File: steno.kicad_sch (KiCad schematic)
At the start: 9 parts, among them SW1 SW_Push, SW2 SW_Push, SW3 SW_Push, SW4 SW_Push, SW5 SW_Push, SW6 SW_Push, SW7 SW_Push, SW8 SW_Push

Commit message: Continue schematic
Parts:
- added SW10, SW11, SW12, SW13, SW14, SW15, SW16, SW17, SW18, SW19, SW20, SW21, SW22, SW23, SW24, SW9: SW_Push, symbol Switch:SW_Push
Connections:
- net S0: now reaches A1.1 (GPIO0)
- net S0: now also SW1.2
- net H: now reaches A1.10 (GPIO7)
- net H: now also SW9.1
- net R: now reaches A1.11 (GPIO8)
- net R: now also SW10.1
- net STAR0: now reaches A1.12 (GPIO9)
- net STAR0: now also SW11.2
- net -A-: now reaches A1.14 (GPIO10)
- net -O-: now reaches A1.15 (GPIO11)
- net -E-: now reaches A1.16 (GPIO12)
- net -U-: now reaches A1.17 (GPIO13)
- net -F: now reaches A1.19 (GPIO14)
- net -F: now also SW20.1
- net S1: now reaches A1.2 (GPIO1)
- net S1: now also SW3.2
- net -R: now reaches A1.20 (GPIO15)
- net -R: now also SW21.1
- net STAR1: now reaches A1.21 (GPIO16)
- net STAR1: now also SW22.2
- net -B: now reaches A1.22 (GPIO17)
- net -B: now also SW18.2
- net -P: now reaches A1.24 (GPIO18)
- net -P: now also SW17.2
- net -G: now reaches A1.25 (GPIO19)
- net -G: now also SW16.1
- net -L: now reaches A1.26 (GPIO20)
- net -L: now also SW15.1
- net -S: now reaches A1.27 (GPIO21)
- net -S: now also SW13.2
- net -T: now reaches A1.29 (GPIO22)
- net -T: now also SW12.2
- net NUM2-3: now reaches A1.31 (GPIO26_ADC0)
- net -Z: now reaches A1.32 (GPIO27_ADC1)
- net -Z: now also SW24.1
- net -D: now reaches A1.34 (GPIO28_ADC2)
- net -D: now also SW23.1
- net T: now reaches A1.4 (GPIO2)
- net T: now also SW4.1
- net K: now reaches A1.5 (GPIO3)
- net K: now also SW5.1
- net NUM0-1: now reaches A1.6 (GPIO4)
- net NUM0-1: now also SW2.2, SW8.1
- net P: now reaches A1.7 (GPIO5)
- net P: now also SW6.2
- net W: now reaches A1.9 (GPIO6)
- net W: now also SW7.2
- net GND: now reaches SW7.1
- net GND: now also SW1.1, SW2.1, SW3.1, SW4.2, SW5.2, SW6.1, SW8.2, SW10.2, SW11.1, SW19.2, SW20.2, SW21.2, SW22.1, SW9.2
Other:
- moved on the sheet: A1, SW1, SW2, SW3, SW4, SW5

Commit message: Start routing
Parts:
- added SW25, SW26, SW27, SW28: SW_Push, Button_Switch_Keyboard:SW_Cherry_MX_1.00u_PCB, symbol Switch:SW_Push
- A1: footprint Module_RaspberryPi_Pico:RaspberryPi_Pico_Common -> PiPico:RaspberryPi_Pico_Common_THT
- SW1, SW10, SW12, SW13, SW15, SW16, SW17, SW18, SW20, SW21, SW23, SW24, SW3, SW4, SW5, SW6, SW7, SW9: footprint (none) -> Button_Switch_Keyboard:SW_Cherry_MX_1.00u_PCB
- SW11, SW14, SW19, SW2, SW22, SW8: footprint (none) -> MX_2U_Modified:SW_Cherry_MX_2.00u_PCB
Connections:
- net -A-: now also SW25.2
- net -D: now also SW23.2; no longer SW23.1
- net -E-: now also SW28.2
- net -F: now also SW20.2; no longer SW20.1
- net -G: now also SW16.2; no longer SW16.1
- net -L: now also SW15.2; no longer SW15.1
- net -O-: now also SW26.2
- net -R: now also SW21.2; no longer SW21.1
- net -U-: now also SW27.2
- net -Z: now also SW24.2; no longer SW24.1
- net GND: now also SW10.1, SW12.1, SW13.1, SW14.1, SW15.1, SW16.1, SW17.1, SW18.1, SW19.1, SW20.1, SW21.1, SW23.1, SW24.1, SW4.1, SW5.1, SW8.1, SW9.1, SW25.1, SW26.1, SW27.1, SW28.1; no longer SW10.2, SW19.2, SW20.2, SW21.2, SW4.2, SW5.2, SW8.2, SW9.2
- net H: now also SW9.2; no longer SW9.1
- net K: now also SW5.2; no longer SW5.1
- net NUM0-1: now also SW8.2; no longer SW8.1
- net NUM2-3: now also SW14.2, SW19.2
- net R: now also SW10.2; no longer SW10.1
- net T: now also SW4.2; no longer SW4.1

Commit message: Finish routing
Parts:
- A1: footprint PiPico:RaspberryPi_Pico_Common_THT -> PiPico:RaspberryPi_Pico_Common
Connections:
- net GND: now also A1.13 (GND), A1.18 (GND), A1.23 (GND), A1.28 (GND), A1.3 (GND), A1.38 (GND), A1.8 (GND)
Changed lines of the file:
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@@
 	(wire
 		(pts
+			(xy 107.95 96.52) (xy 107.95 99.06)
+		)
+		(stroke
+			(width 0)
+			(type default)
+		)
+	)
+	(wire
+		(pts
 			(xy 68.58 125.73) (xy 71.12 125.73)
 		)
@@
 			)
 		)
-		(property "Footprint" "PiPico:RaspberryPi_Pico_Common_THT"
+		(property "Footprint" "PiPico:RaspberryPi_Pico_Common"
 			(at 107.95 107.95 0)
 			(effects
@@
 					(unit 1)
 				)
+			)
+		)
+	)
+	(symbol
+		(lib_id "power:GND")
+		(at 107.95 99.06 0)
+		(unit 1)
+		(exclude_from_sim no)
+		(in_bom yes)
+		(on_board yes)
+		(dnp no)
+		(property "Reference" "#PWR08"
+			(at 107.95 105.41 0)
+			(effects
+				(font
+					(size 1.27 1.27)
+				)
+				(hide yes)
+			)
+		)
+		(property "Value" "GND"
+			(at 107.95 102.87 0)
+			(effects
+				(font
+					(size 1.27 1.27)
+				)
+			)
+		)
+		(property "Footprint" ""
+			(at 107.95 99.06 0)
+			(effects
+				(font
+					(size 1.27 1.27)
+				)
+				(hide yes)
+			)
+		)
+		(property "Datasheet" ""
+			(at 107.95 99.06 0)
+			(effects
+				(font
+					(size 1.27 1.27)
+				)
+				(hide yes)
+			)
+		)
+		(property "Description" "Power symbol creates a global label with name \"GND\" , ground"
+			(at 107.95 99.06 0)
+			(effects
+				(font
+					(size 1.27 1.27)
+				)
+				(hide yes)
+			)
+		)
+		(pin "1"
+		)
+		(instances
+			(project ""
+				(path "/81be89d4-c12a-4c6e-a91b-ff1d6efea102"
+					(reference "#PWR08")
+					(unit 1)
+				)

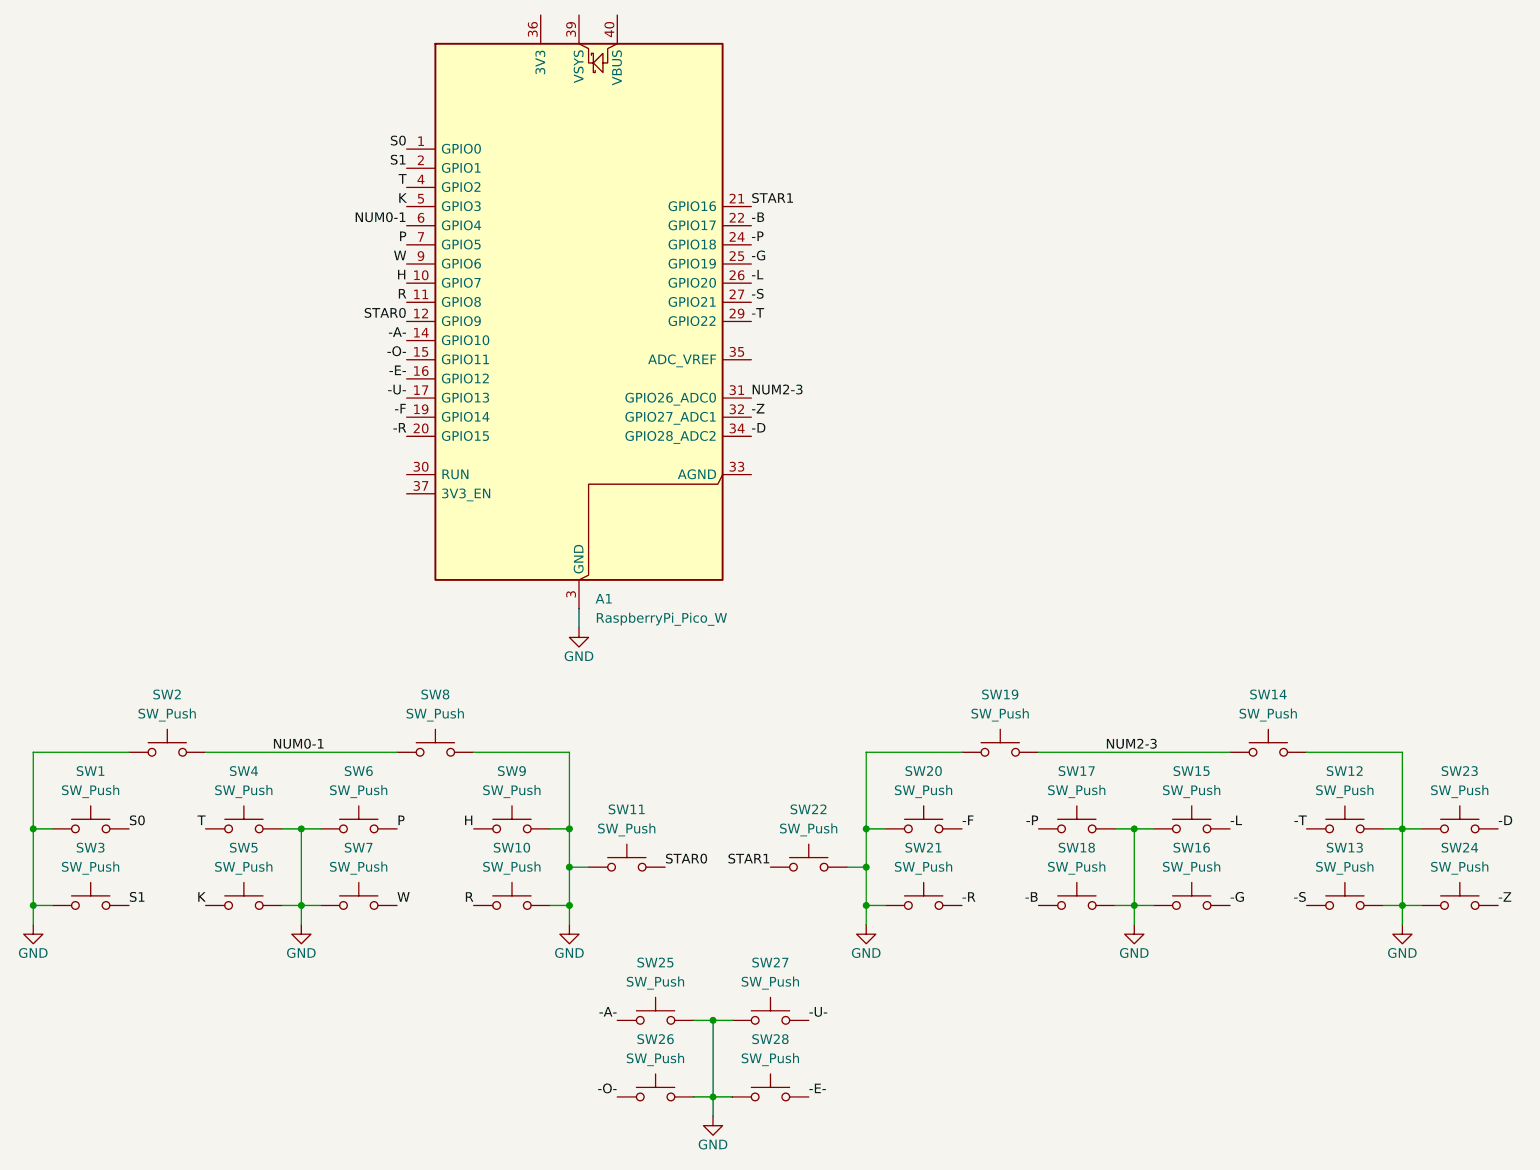
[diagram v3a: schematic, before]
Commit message: Finalized routing, added mounting holes
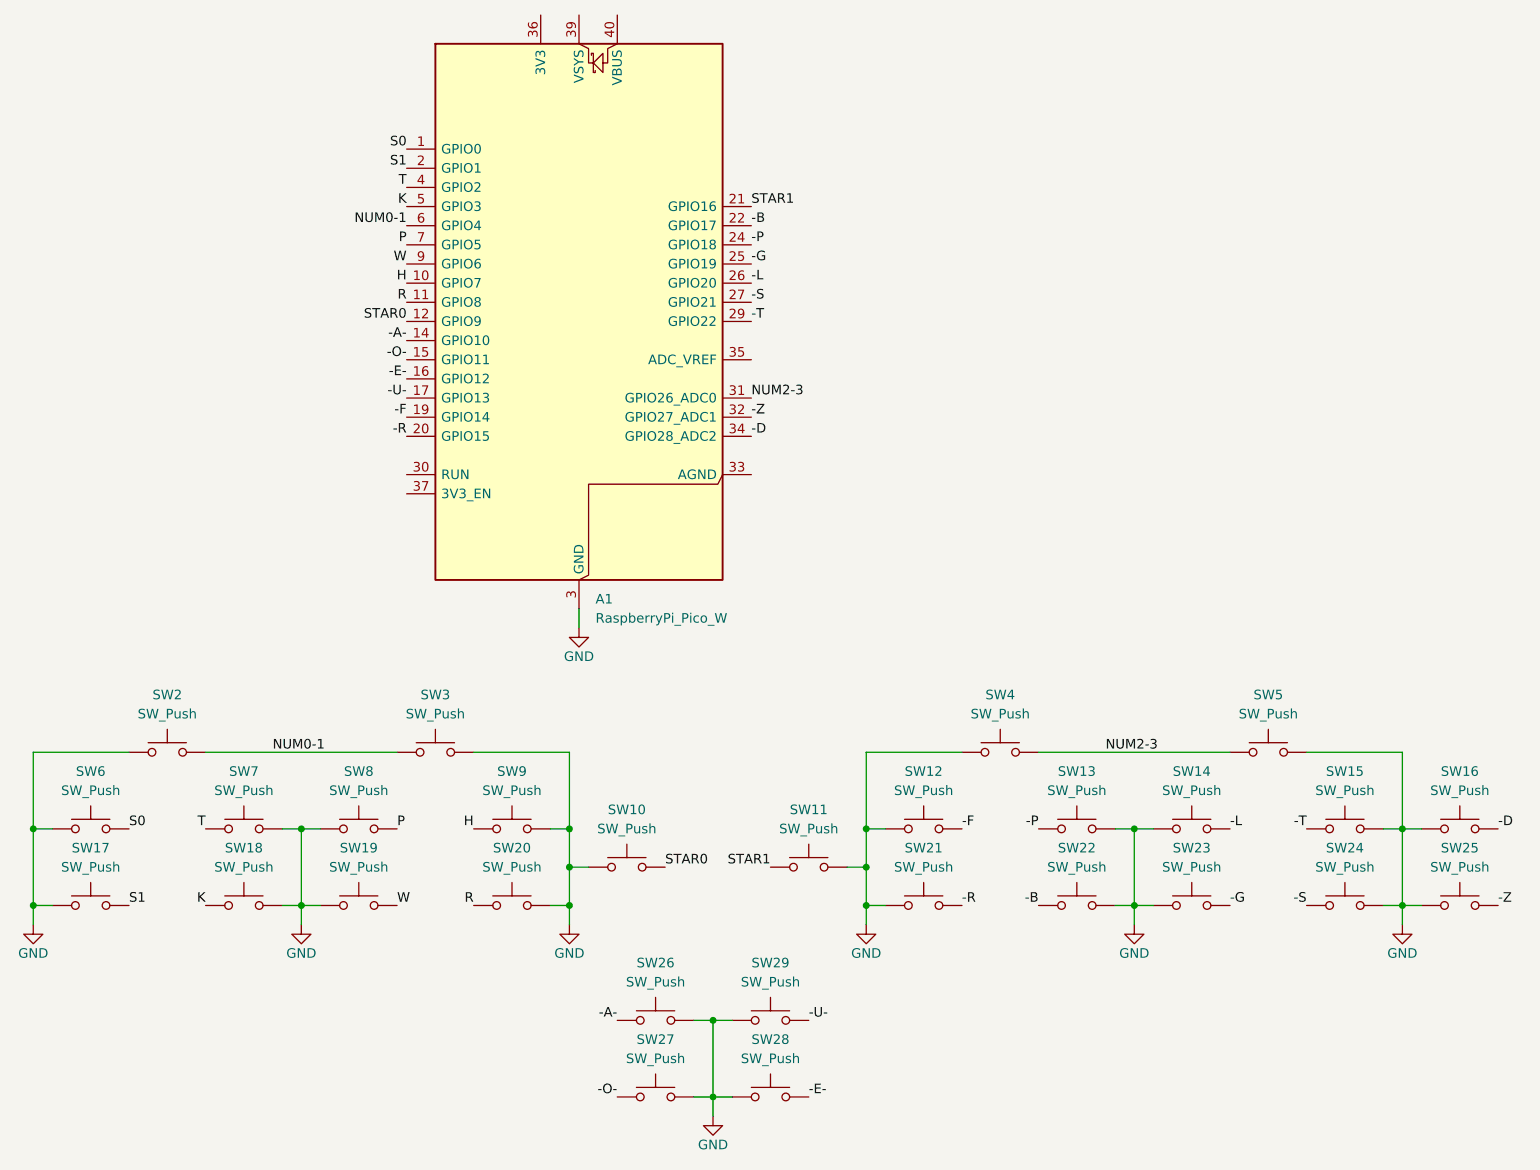
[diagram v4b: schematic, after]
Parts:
- renumbered SW11 to SW10, SW22 to SW11, SW20 to SW12, SW17 to SW13, SW15 to SW14, SW12 to SW15, SW23 to SW16, SW3 to SW17, SW5 to SW18, SW7 to SW19, SW10 to SW20, SW18 to SW22, SW16 to SW23, SW13 to SW24, SW24 to SW25, SW25 to SW26, SW26 to SW27, SW27 to SW29, SW8 to SW3, SW19 to SW4, SW14 to SW5, SW1 to SW6, SW4 to SW7, SW6 to SW8
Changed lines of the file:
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@@
 		(on_board yes)
 		(dnp no)
-		(property "Reference" "SW8"
+		(property "Reference" "SW3"
 			(at 88.9 107.95 0)
 			(effects
@@
 			(project "steno"
 				(path "/81be89d4-c12a-4c6e-a91b-ff1d6efea102"
-					(reference "SW8")
+					(reference "SW3")
 					(unit 1)
 				)
@@
 		(dnp no)
 		(fields_autoplaced yes)
-		(property "Reference" "SW13"
+		(property "Reference" "SW24"
 			(at 209.55 128.27 0)
 			(effects
@@
 			(project "steno"
 				(path "/81be89d4-c12a-4c6e-a91b-ff1d6efea102"
-					(reference "SW13")
+					(reference "SW24")
 					(unit 1)
 				)
@@
 		(dnp no)
 		(fields_autoplaced yes)
-		(property "Reference" "SW6"
+		(property "Reference" "SW8"
 			(at 78.74 118.11 0)
 			(effects
@@
 			(project "steno"
 				(path "/81be89d4-c12a-4c6e-a91b-ff1d6efea102"
-					(reference "SW6")
+					(reference "SW8")
 					(unit 1)
 				)
@@
 		(on_board yes)
 		(dnp no)
-		(property "Reference" "SW16"
+		(property "Reference" "SW23"
 			(at 189.23 128.27 0)
 			(effects
@@
 			(project "steno"
 				(path "/81be89d4-c12a-4c6e-a91b-ff1d6efea102"
-					(reference "SW16")
+					(reference "SW23")
 					(unit 1)
 				)
@@
 		(dnp no)
 		(fields_autoplaced yes)
-		(property "Reference" "SW11"
+		(property "Reference" "SW10"
 			(at 114.3 123.19 0)
 			(effects
@@
 			(project "steno"
 				(path "/81be89d4-c12a-4c6e-a91b-ff1d6efea102"
-					(reference "SW11")
+					(reference "SW10")
 					(unit 1)
 				)
@@
 		(on_board yes)
 		(dnp no)
-		(property "Reference" "SW22"
+		(property "Reference" "SW11"
 			(at 138.43 123.19 0)
 			(effects
@@
 			(project "steno"
 				(path "/81be89d4-c12a-4c6e-a91b-ff1d6efea102"
-					(reference "SW22")
+					(reference "SW11")
 					(unit 1)
 				)
@@
 		(on_board yes)
 		(dnp no)
-		(property "Reference" "SW20"
+		(property "Reference" "SW12"
 			(at 153.67 118.11 0)
 			(effects
@@
 			(project "steno"
 				(path "/81be89d4-c12a-4c6e-a91b-ff1d6efea102"
-					(reference "SW20")
+					(reference "SW12")
 					(unit 1)
 				)
@@
 		(on_board yes)
 		(dnp no)
-		(property "Reference" "SW26"
+		(property "Reference" "SW27"
 			(at 118.11 153.67 0)
 			(effects
@@
 			(project "steno"
 				(path "/81be89d4-c12a-4c6e-a91b-ff1d6efea102"
-					(reference "SW26")
+					(reference "SW27")
 					(unit 1)
 				)
@@
 		(on_board yes)
 		(dnp no)
-		(property "Reference" "SW10"
+		(property "Reference" "SW20"
 			(at 99.06 128.27 0)
 			(effects
@@
 			(project "steno"
 				(path "/81be89d4-c12a-4c6e-a91b-ff1d6efea102"
-					(reference "SW10")
+					(reference "SW20")
 					(unit 1)
 				)
@@
 		(on_board yes)
 		(dnp no)
-		(property "Reference" "SW4"
+		(property "Reference" "SW7"
 			(at 63.5 118.11 0)
 			(effects
@@
 			(project "steno"
 				(path "/81be89d4-c12a-4c6e-a91b-ff1d6efea102"
-					(reference "SW4")
+					(reference "SW7")
 					(unit 1)
 				)
@@
 		(on_board yes)
 		(dnp no)
-		(property "Reference" "SW25"
+		(property "Reference" "SW26"
 			(at 118.11 143.51 0)
 			(effects
@@
 			(project "steno"
 				(path "/81be89d4-c12a-4c6e-a91b-ff1d6efea102"
-					(reference "SW25")
+					(reference "SW26")
 					(unit 1)
 				)
@@
 		(on_board yes)
 		(dnp no)
-		(property "Reference" "SW5"
+		(property "Reference" "SW18"
 			(at 63.5 128.27 0)
 			(effects
@@
 			(project "steno"
 				(path "/81be89d4-c12a-4c6e-a91b-ff1d6efea102"
-					(reference "SW5")
+					(reference "SW18")
 					(unit 1)
 				)
@@
 		(dnp no)
 		(fields_autoplaced yes)
-		(property "Reference" "SW1"
+		(property "Reference" "SW6"
 			(at 43.18 118.11 0)
 			(effects
@@
 			(project ""
 				(path "/81be89d4-c12a-4c6e-a91b-ff1d6efea102"
-					(reference "SW1")
+					(reference "SW6")
 					(unit 1)
 				)
@@
 		(dnp no)
 		(fields_autoplaced yes)
-		(property "Reference" "SW12"
+		(property "Reference" "SW15"
 			(at 209.55 118.11 0)
 			(effects
@@
 			(project "steno"
 				(path "/81be89d4-c12a-4c6e-a91b-ff1d6efea102"
-					(reference "SW12")
+					(reference "SW15")
 					(unit 1)
 				)
@@
 		(on_board yes)
 		(dnp no)
-		(property "Reference" "SW15"
+		(property "Reference" "SW14"
 			(at 189.23 118.11 0)
 			(effects
@@
 			(project "steno"
 				(path "/81be89d4-c12a-4c6e-a91b-ff1d6efea102"
-					(reference "SW15")
+					(reference "SW14")
 					(unit 1)
 				)
@@
 		(dnp no)
 		(fields_autoplaced yes)
-		(property "Reference" "SW7"
+		(property "Reference" "SW19"
 			(at 78.74 128.27 0)
 			(effects
@@
 			(project "steno"
 				(path "/81be89d4-c12a-4c6e-a91b-ff1d6efea102"
-					(reference "SW7")
+					(reference "SW19")
 					(unit 1)
 				)
@@
 		(on_board yes)
 		(dnp no)
-		(property "Reference" "SW24"
+		(property "Reference" "SW25"
 			(at 224.79 128.27 0)
 			(effects
@@
 			(project "steno"
 				(path "/81be89d4-c12a-4c6e-a91b-ff1d6efea102"
-					(reference "SW24")
+					(reference "SW25")
 					(unit 1)
 				)
@@
 		(on_board yes)
 		(dnp no)
-		(property "Reference" "SW27"
+		(property "Reference" "SW29"
 			(at 133.35 143.51 0)
 			(effects
@@
 			(project "steno"
 				(path "/81be89d4-c12a-4c6e-a91b-ff1d6efea102"
-					(reference "SW27")
+					(reference "SW29")
 					(unit 1)
 				)
@@
 		(on_board yes)
 		(dnp no)
-		(property "Reference" "SW14"
+		(property "Reference" "SW5"
 			(at 199.39 107.95 0)
 			(effects
@@
 			(project "steno"
 				(path "/81be89d4-c12a-4c6e-a91b-ff1d6efea102"
-					(reference "SW14")
+					(reference "SW5")
 					(unit 1)
 				)
@@
 		(dnp no)
 		(fields_autoplaced yes)
-		(property "Reference" "SW18"
+		(property "Reference" "SW22"
 			(at 173.99 128.27 0)
 			(effects
@@
 			(project "steno"
 				(path "/81be89d4-c12a-4c6e-a91b-ff1d6efea102"
-					(reference "SW18")
+					(reference "SW22")
 					(unit 1)
 				)
@@
 		(dnp no)
 		(fields_autoplaced yes)
-		(property "Reference" "SW3"
+		(property "Reference" "SW17"
 			(at 43.18 128.27 0)
 			(effects
@@
 			(project "steno"
 				(path "/81be89d4-c12a-4c6e-a91b-ff1d6efea102"
-					(reference "SW3")
+					(reference "SW17")
 					(unit 1)
 				)
@@
 		(on_board yes)
 		(dnp no)
-		(property "Reference" "SW23"
+		(property "Reference" "SW16"
 			(at 224.79 118.11 0)
 			(effects
@@
 			(project "steno"
 				(path "/81be89d4-c12a-4c6e-a91b-ff1d6efea102"
-					(reference "SW23")
+					(reference "SW16")
 					(unit 1)
 				)
@@
 		(on_board yes)
 		(dnp no)
-		(property "Reference" "SW19"
+		(property "Reference" "SW4"
 			(at 163.83 107.95 0)
 			(effects
@@
 			(project "steno"
 				(path "/81be89d4-c12a-4c6e-a91b-ff1d6efea102"
-					(reference "SW19")
+					(reference "SW4")
 					(unit 1)
 				)
@@
 		(dnp no)
 		(fields_autoplaced yes)
-		(property "Reference" "SW17"
+		(property "Reference" "SW13"
 			(at 173.99 118.11 0)
 			(effects
@@
 			(project "steno"
 				(path "/81be89d4-c12a-4c6e-a91b-ff1d6efea102"
-					(reference "SW17")
-					(unit 1)
-				)
+					(reference "SW13")
+					(unit 1)
+				)

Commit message: Finalised design
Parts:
- SW1: renamed from SW2; footprint MX_2U_Modified:SW_Cherry_MX_2.00u_PCB -> MX_Modified:SW_Cherry_MX_2.00u_PCB
- SW10: renamed from SW11; footprint MX_2U_Modified:SW_Cherry_MX_2.00u_PCB -> MX_Modified:SW_Cherry_MX_2.00u_PCB
- SW11: renamed from SW12; footprint Button_Switch_Keyboard:SW_Cherry_MX_1.00u_PCB -> MX_Modified:SW_Cherry_MX_1.00u_PCB
- SW12: renamed from SW13; footprint Button_Switch_Keyboard:SW_Cherry_MX_1.00u_PCB -> MX_Modified:SW_Cherry_MX_1.00u_PCB
- SW13: renamed from SW14; footprint Button_Switch_Keyboard:SW_Cherry_MX_1.00u_PCB -> MX_Modified:SW_Cherry_MX_1.00u_PCB
- SW14: renamed from SW15; footprint Button_Switch_Keyboard:SW_Cherry_MX_1.00u_PCB -> MX_Modified:SW_Cherry_MX_1.00u_PCB
- SW15: renamed from SW16; footprint Button_Switch_Keyboard:SW_Cherry_MX_1.00u_PCB -> MX_Modified:SW_Cherry_MX_1.00u_PCB
- SW16: renamed from SW17; footprint Button_Switch_Keyboard:SW_Cherry_MX_1.00u_PCB -> MX_Modified:SW_Cherry_MX_1.00u_PCB
- SW17: renamed from SW18; footprint Button_Switch_Keyboard:SW_Cherry_MX_1.00u_PCB -> MX_Modified:SW_Cherry_MX_1.00u_PCB
- SW18: renamed from SW19; footprint Button_Switch_Keyboard:SW_Cherry_MX_1.00u_PCB -> MX_Modified:SW_Cherry_MX_1.00u_PCB
- SW19: renamed from SW20; footprint Button_Switch_Keyboard:SW_Cherry_MX_1.00u_PCB -> MX_Modified:SW_Cherry_MX_1.00u_PCB
- SW2: renamed from SW3; footprint MX_2U_Modified:SW_Cherry_MX_2.00u_PCB -> MX_Modified:SW_Cherry_MX_2.00u_PCB
- SW20: renamed from SW21; footprint Button_Switch_Keyboard:SW_Cherry_MX_1.00u_PCB -> MX_Modified:SW_Cherry_MX_1.00u_PCB
- SW21: renamed from SW22; footprint Button_Switch_Keyboard:SW_Cherry_MX_1.00u_PCB -> MX_Modified:SW_Cherry_MX_1.00u_PCB
- SW22: renamed from SW23; footprint Button_Switch_Keyboard:SW_Cherry_MX_1.00u_PCB -> MX_Modified:SW_Cherry_MX_1.00u_PCB
- SW23: renamed from SW24; footprint Button_Switch_Keyboard:SW_Cherry_MX_1.00u_PCB -> MX_Modified:SW_Cherry_MX_1.00u_PCB
- SW24: renamed from SW25; footprint Button_Switch_Keyboard:SW_Cherry_MX_1.00u_PCB -> MX_Modified:SW_Cherry_MX_1.00u_PCB
- SW25: renamed from SW26; footprint Button_Switch_Keyboard:SW_Cherry_MX_1.00u_PCB -> MX_Modified:SW_Cherry_MX_1.00u_PCB
- SW26: renamed from SW27; footprint Button_Switch_Keyboard:SW_Cherry_MX_1.00u_PCB -> MX_Modified:SW_Cherry_MX_1.00u_PCB
- SW27: renamed from SW28; footprint Button_Switch_Keyboard:SW_Cherry_MX_1.00u_PCB -> MX_Modified:SW_Cherry_MX_1.00u_PCB
- SW28: renamed from SW29; footprint Button_Switch_Keyboard:SW_Cherry_MX_1.00u_PCB -> MX_Modified:SW_Cherry_MX_1.00u_PCB
- SW3: renamed from SW4; footprint MX_2U_Modified:SW_Cherry_MX_2.00u_PCB -> MX_Modified:SW_Cherry_MX_2.00u_PCB
- SW4: renamed from SW5; footprint MX_2U_Modified:SW_Cherry_MX_2.00u_PCB -> MX_Modified:SW_Cherry_MX_2.00u_PCB
- SW5: renamed from SW6; footprint Button_Switch_Keyboard:SW_Cherry_MX_1.00u_PCB -> MX_Modified:SW_Cherry_MX_1.00u_PCB
- SW6: renamed from SW7; footprint Button_Switch_Keyboard:SW_Cherry_MX_1.00u_PCB -> MX_Modified:SW_Cherry_MX_1.00u_PCB
- SW7: renamed from SW8; footprint Button_Switch_Keyboard:SW_Cherry_MX_1.00u_PCB -> MX_Modified:SW_Cherry_MX_1.00u_PCB
- SW8: renamed from SW9; footprint Button_Switch_Keyboard:SW_Cherry_MX_1.00u_PCB -> MX_Modified:SW_Cherry_MX_1.00u_PCB
- SW9: renamed from SW10; footprint MX_2U_Modified:SW_Cherry_MX_2.00u_PCB -> MX_Modified:SW_Cherry_MX_2.00u_PCB
